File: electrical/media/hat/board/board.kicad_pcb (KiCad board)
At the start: 2 copper layers, 33 x 24.5 mm, 9 parts, among them J101 RPI_PINS, J102 5V_IN, SW101 TS50810-411-02528

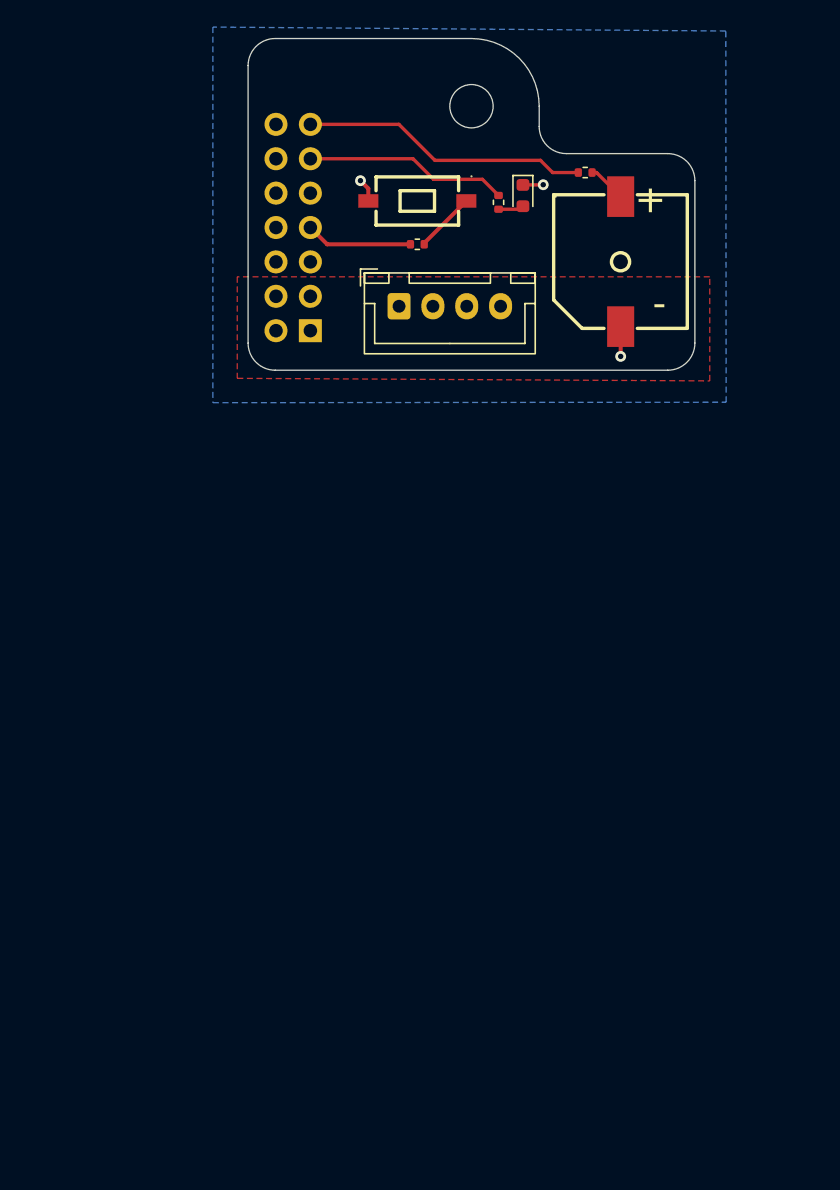
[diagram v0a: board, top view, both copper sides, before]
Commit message: media hat power fix fabrication ready
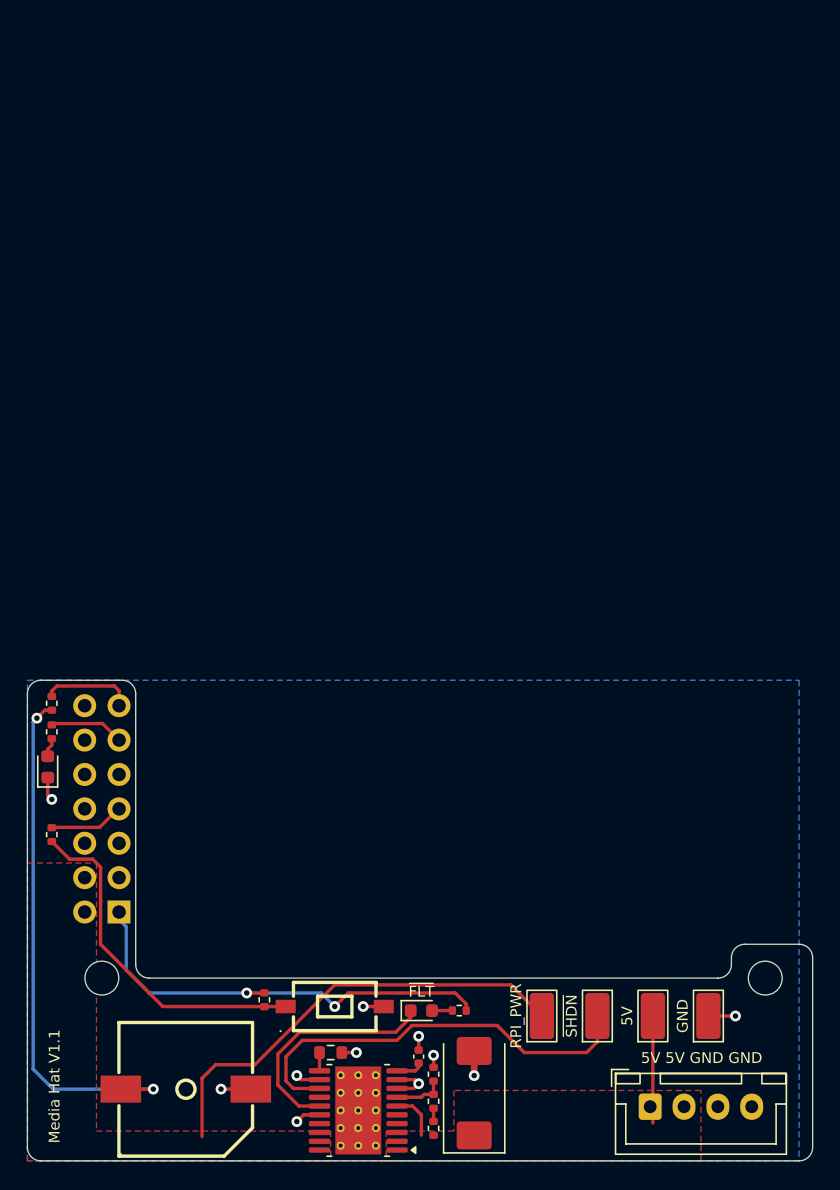
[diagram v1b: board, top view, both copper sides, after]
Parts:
- added C101: 100u, Capacitor_Tantalum_SMD:CP_EIA-7343-31_Kemet-D, F.Cu at (93.5, 137.5)
- added C102: 22n, Capacitor_SMD:C_0402_1005Metric, F.Cu at (89.4, 134.8)
- added D102: LED, LED_SMD:LED_0603_1608Metric, F.Cu at (89.6, 131.4)
- added H102: MountingHole, MountingHole:MountingHole_2.5mm, F.Cu at (115.0, 129.0)
- added R104: 2.2k, Resistor_SMD:R_0402_1005Metric, F.Cu at (78.0, 130.6)
- added R105: 2.2k, Resistor_SMD:R_0402_1005Metric, F.Cu at (92.4, 131.4)
- added R106: 3k, Resistor_SMD:R_0603_1608Metric, F.Cu at (82.9, 134.5)
- added R107: 1.2k, Resistor_SMD:R_0402_1005Metric, F.Cu at (90.5, 136.1)
- added R108: 2.2k, Resistor_SMD:R_0402_1005Metric, F.Cu at (90.5, 138.1)
- added R109: 1.2k, Resistor_SMD:R_0402_1005Metric, F.Cu at (90.5, 140.1)
- added TP101: ~{SHDN} Test Point, TestPoint:TestPoint_Keystone_5015_Micro_Mini, F.Cu at (102.6, 131.8)
- added TP102: GND Test Point, TestPoint:TestPoint_Keystone_5015_Micro_Mini, F.Cu at (110.8, 131.8)
- added TP103: 5V Test Point, TestPoint:TestPoint_Keystone_5015_Micro_Mini, F.Cu at (106.7, 131.8)
- added TP104: RPI PWR Test Point, TestPoint:TestPoint_Keystone_5015_Micro_Mini, F.Cu at (98.5, 131.8)
- added U101: TPS26631PWP, Package_SO:HTSSOP-20-1EP_4.4x6.5mm_P0.65mm_EP3.4x6.5mm_Mask2.96x2.96mm_ThermalVias, F.Cu at (84.9, 138.8)
- H101: footprint MountingHole:MountingHole_3.2mm_M3 -> MountingHole:MountingHole_2.5mm
- R102: value 430 -> 100
- moved H101 69.9 mm to (66.0, 129.0)
- moved BUZZER101 69.0 mm to (72.2, 137.2), turned to -90 degrees
- moved J102 62.0 mm to (106.5, 138.5)
- moved SW101 59.8 mm to (83.2, 131.1), turned to 0 degrees
- moved R102 55.6 mm to (62.3, 108.7), turned to 90 degrees
- moved D101 54.9 mm to (62.0, 113.4), turned to 90 degrees
- moved R101 51.3 mm to (62.3, 118.4), turned to -90 degrees
- moved R103 51.2 mm to (62.3, 110.8)
- moved J101 45.2 mm to (67.3, 124.1)
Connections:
- J101 pad 1: unconnected-(J101-Pin_1-Pad1) -> +3V3
- J101 pad 2: +5V -> /RPI_PWR
- J101 pad 4: +5V -> /RPI_PWR
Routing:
- net Net-(BUZZER101-+): track 2.85 -> 39.3 mm, vias 0 -> 2
- net +3V3: track 0.00 -> 33.3 mm, vias 0 -> 2
- net /RPI_PWR: track 0.00 -> 33.2 mm
- net Net-(U101-~{SHDN}): track 0.00 -> 31.5 mm
- net Net-(R101-Pad2): track 4.49 -> 25.7 mm
- net Net-(D102-K): track 0.00 -> 17.4 mm
- net /GPIO27: track 21.3 -> 6.77 mm
- net GND: track 5.45 -> 19.4 mm, vias 3 -> 11
- net +5V: track 0.00 -> 11.5 mm
- net /GPIO17: track 15.0 -> 5.52 mm
- net Net-(U101-UVLO): track 0.00 -> 3.77 mm
- net /GPIO4: track 7.90 -> 5.60 mm
- net Net-(U101-dVdT): track 0.00 -> 2.02 mm
- net Net-(D102-A): track 0.00 -> 1.50 mm
- net Net-(U101-ILIM): track 0.00 -> 1.35 mm
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- added copper zone on F.Cu, net /RPI_PWR
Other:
- board size 33 x 24.5 mm -> 58 x 35.5 mm
- board text added: "5V"
- board text added: "5V 5V GND GND"
- board text added: "GND"
- board text added: "Media Hat V1.1"
- board text added: "RPI_PWR"
- board text added: "~{FLT}"
- board text added: "~{SHDN}"
- board text removed: "ASV1_700 RPI-HAT-V1.1"

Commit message: flip connector polarity
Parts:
- moved J102 7.54 mm to (114.0, 139.3), turned to 180 degrees
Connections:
- J102 pad 1: +5V -> GND
- J102 pad 2: +5V -> GND
- J102 pad 3: GND -> +5V
- J102 pad 4: GND -> +5V
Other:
- board text added: "Media Hat V1.2"
- board text removed: "Media Hat V1.1"

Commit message: change FLT to RED LED
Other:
- board text added: "FLT"
- board text removed: "~{FLT}"
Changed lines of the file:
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@@
 		(layer "User.1")
 	)
-	(gr_text "~{FLT}"
+	(gr_text "FLT"
 		(at 89.6 130 0)
 		(layer "F.SilkS")
@@
 	)
 	(segment
+		(start 106.7 131.8)
+		(end 106.7 139.7)
+		(width 0.25)
+		(layer "F.Cu")
+		(net "+5V")
+	)
+	(segment
+		(start 88.95 138.45)
+		(end 89.6 139.1)
+		(width 0.25)
+		(layer "F.Cu")
+		(net "+5V")
+	)
+	(segment
+		(start 89.6 139.1)
+		(end 89.6 140.6)
+		(width 0.25)
+		(layer "F.Cu")
+		(net "+5V")
+	)
+	(segment
+		(start 87.8 138.45)
+		(end 88.95 138.45)
+		(width 0.25)
+		(layer "F.Cu")
+		(net "+5V")
+	)
+	(segment
 		(start 61.79 109.21)
 		(end 61.2 109.8)
@@
 	)
 	(segment
-		(start 106.7 131.8)
-		(end 106.7 139.7)
-		(width 0.25)
-		(layer "F.Cu")
-		(net "+5V")
-	)
-	(segment
-		(start 88.95 138.45)
-		(end 89.6 139.1)
-		(width 0.25)
-		(layer "F.Cu")
-		(net "+5V")
-	)
-	(segment
-		(start 89.6 139.1)
-		(end 89.6 140.6)
-		(width 0.25)
-		(layer "F.Cu")
-		(net "+5V")
-	)
-	(segment
-		(start 87.8 138.45)
-		(end 88.95 138.45)
-		(width 0.25)
-		(layer "F.Cu")
-		(net "+5V")
-	)
-	(segment

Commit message: LCSC number fix
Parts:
- D101: value LED -> Green LED
- D102: value LED -> Red LED
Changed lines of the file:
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@@
 			)
 		)
-		(property "Value" "LED"
+		(property "Value" "Green LED"
 			(at 0 1.43 90)
 			(layer "F.Fab")
@@
 			)
 		)
-		(property "Value" "LED"
+		(property "Value" "Red LED"
 			(at 0 1.43 0)
 			(layer "F.Fab")
@@
 			)
 		)
-		(property "LCSC" "C965804"
+		(property "LCSC" "C2286"
 			(at 0 0 0)
 			(unlocked yes)
